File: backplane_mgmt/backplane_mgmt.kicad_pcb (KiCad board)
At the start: 2 copper layers, 160 x 100 mm, 113 parts, among them J101 AudioJack3, J201 Backplane, J304 VIn, Q301 SUD19P06-60, Q302 SUD19P06-60, Q401 PSMN045-80YS, Q402 PSMN045-80YS, U101 LM833, U203 AT24CS32-SSHM, U301 AZ1117CD-5.0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

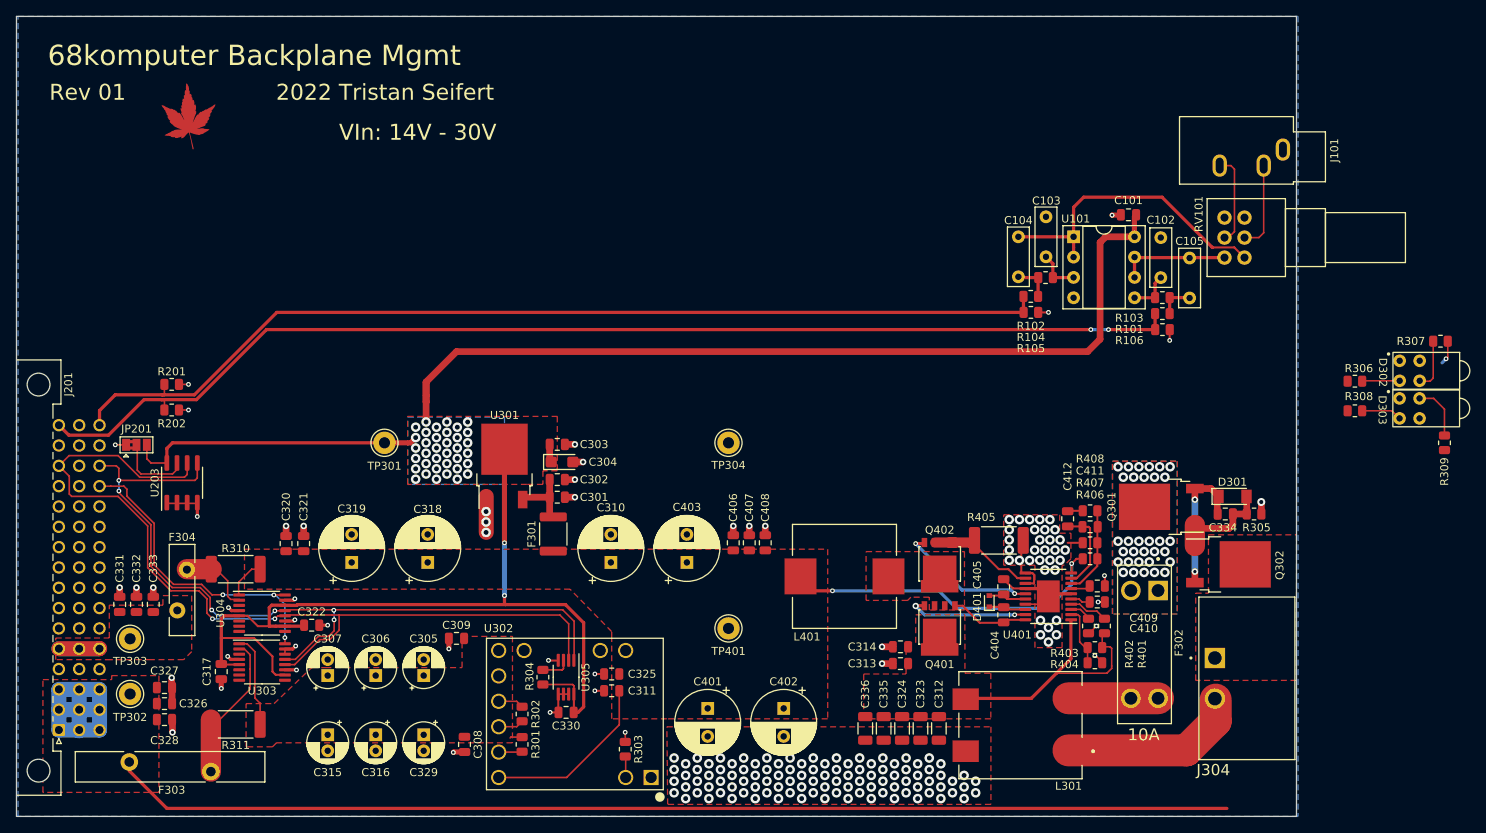
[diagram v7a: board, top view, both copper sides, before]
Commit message: Minor layout tweaks across the board
- Added an input for a test clock, and a jumper for sending this clock
  instead of the CPU clock to the clock pins of the expansion cards on
  the backplane boards

- Reworked a bunch of the power supply board

- Minor changes (to consolidate BOMs) on CPU board for some capacitors,
  they were replaced with SMD versions
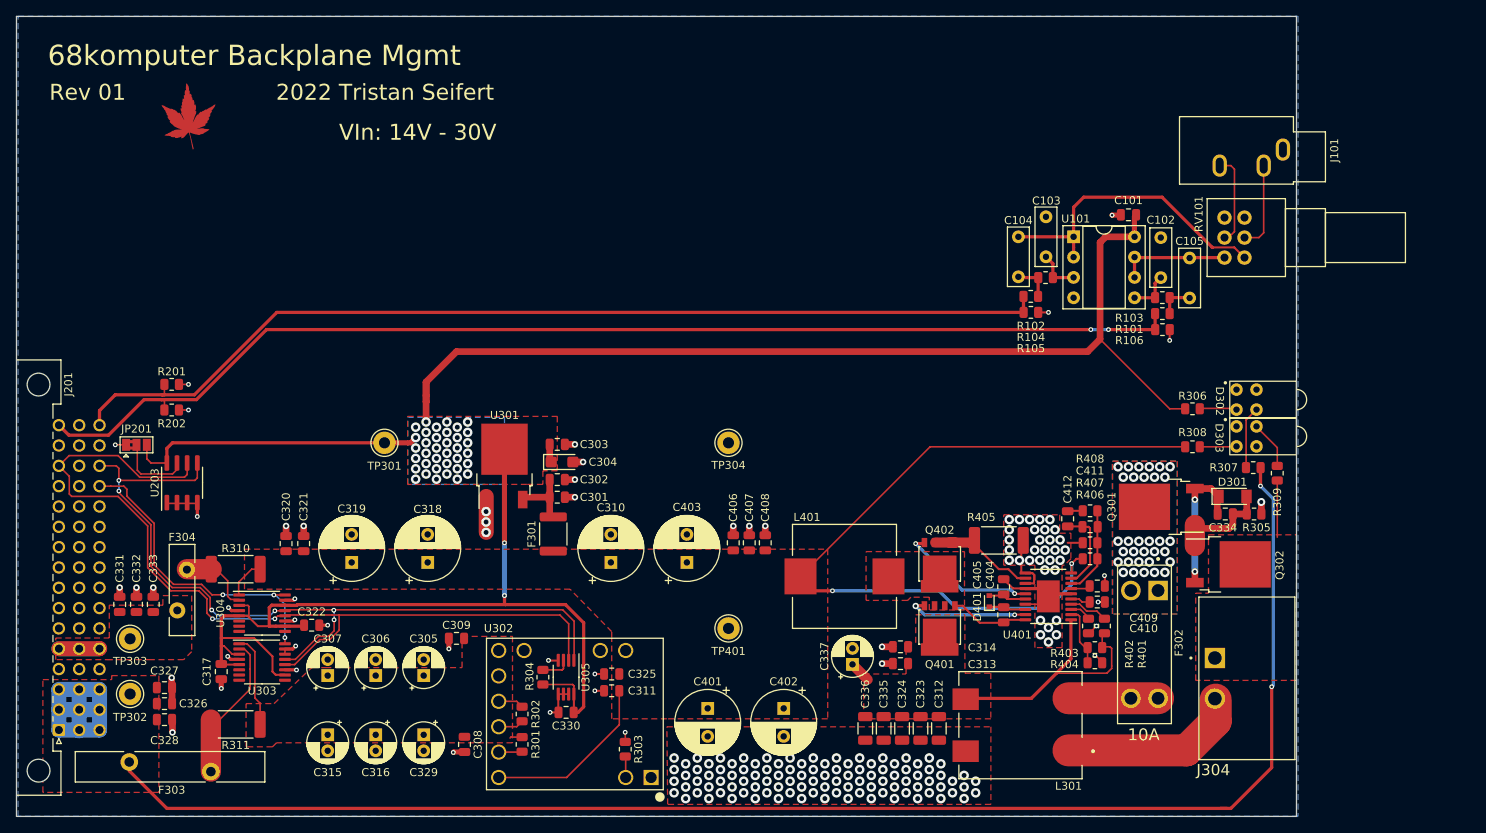
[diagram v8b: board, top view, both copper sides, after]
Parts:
- added C337: 22µF, Capacitor_THT:CP_Radial_D5.0mm_P2.00mm, F.Cu at (134.5, 101.0)
- moved R307 28.2 mm to (184.6, 76.4)
- moved R309 21.2 mm to (187.6, 77.1)
- moved R308 20.8 mm to (177.0, 73.8)
- moved D302 20.7 mm to (190.0, 67.9)
- moved D303 20.7 mm to (190.0, 72.5)
- moved R306 20.6 mm to (177.0, 69.0)
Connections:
- R308 pad 2: VBUS -> VDD
- U303 pad 3: unconnected-(U303-Pad3) -> +5VA
- U304 pad 3: unconnected-(U304-Pad3) -> +5VA
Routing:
- net VDD: track 69.1 -> 123.9 mm
- net +5V: track 174.3 -> 218.0 mm, vias 1 -> 2
- net +5VA: track 269.0 -> 288.5 mm
- net /Power/VIn: track 0.00 -> 7.09 mm
- net VBUS: track 32.7 -> 35.4 mm
- net Net-(D302-Pad1): track 6.46 -> 7.79 mm
- net Net-(D303-Pad3): track 6.96 -> 5.96 mm
